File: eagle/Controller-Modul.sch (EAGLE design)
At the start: 53 parts, among them IC2 7805TV, Q6 BC550C, Q7 BC560, U1 ATTINY85-20S, X1 MKDSN1,5/2-5,08, X2 MKDSN1,5/2-5,08, X4 MKDSN1,5/2-5,08

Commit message: pcb design
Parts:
- removed C1, C5, C6: 100nF, rcl:C-EUC0805
- removed C2: 100µ, resistor:CPOL-EUE2.5-7
- removed C3: (no value), rcl:C-EUC0603K
- removed C4: 1000µ, rcl:CPOL-EUE3.5-8
- removed D1: 18V, diode:ZENER-DIODESOD80C
- removed D2: (no value), diode:ZENER-DIODESOT23
- removed D3: 1N4004, diode:1N4004
- removed IC1: (no value), v-reg:LM317TS
- removed IC2: 7805TV, linear:7805TV
- removed LED1: (no value), led:LED3MM
- removed Q2, Q3, Q4, Q5: (no value), transistor-power:PMOSFET_NTO220BV
- removed Q6: BC550C, transistor-npn:BC550C
- removed Q7: BC560, transistor-pnp:BC560
- removed R15: 1k, resistor:R-EU_R1206
- removed R16, R18, R19: 33k, resistor:R-EU_R1206
- removed R17: 10k, resistor:R-EU_R1206
- removed R20: 100k, rcl:R-EU_R1206
- removed R21: (no value), pot:TRIM_EU-PT10
- removed R5, R6, R7: (no value), resistor:R-EU_0207/10
- removed TR1, TR2: (no value), trafo:EI38-1
- removed U$1: GLEICHRICHTER, Gleichrichter:GLEICHRICHTER
- removed U1: ATTINY85-20S, _hhn_attiny25_45_85:ATTINY85-20S
- removed X1, X2, X4: MKDSN1,5/2-5,08, con-phoenix-508:MKDSN1,5/2-5,08
- added 1: SUMMER4, 0liver:SUMMER4
- added C10, C11: 22pF, resistor:C-EUC0603K
- added C12: 100 nF, resistor:C-EUC0603
- added C9: 1n, rcl:C-EUC0603K
- added D4, D5, D6: (no value), diode:ZENER-DIODESOT23
- added IC3: ATMEGA328P, avr-6:MEGA48/88/168-PU
- added JP10, JP4, JP6: (no value), pinhead:PINHD-1X2
- added JP5: (no value), pinhead:PINHD-1X4
- added JP7: (no value), pinhead:PINHD-1X16
- added JP8: (no value), pinhead:PINHD-2X3
- added JP9: (no value), pinhead:PINHD-1X3
- C7: value 100nF -> 1n; device rcl:C-EUC0805 -> rcl:C-EUC0603K
- C8: value 100µ -> 1n; device rcl:CPOL-EUE3.5-8 -> rcl:C-EUC0603K
- JP2: device pinhead:PINHD-2X3 -> pinhead:PINHD-1X2
- Q1: value (none) -> BC550C; device transistor-power:PMOSFET_NTO220BV -> transistor-npn:BC550C
- R10, R8: value (none) -> 300; device resistor:R-EU_0207/10 -> resistor:R-EU_R1206
- R11: value (none) -> 10k; device resistor:R-EU_0207/10 -> pot:TRIM_EU-PT10
- R12: value 100k -> 2k7; device rcl:R-EU_R1206 -> resistor:R-EU_R1206
- R13: value 10k -> 300
- R14: value 33k -> 2k7
- R2: value (none) -> 10k; device resistor:R-EU_0207/10 -> resistor:R-EU_R1206
- R3: value (none) -> 33k; device resistor:R-EU_0207/10 -> resistor:R-EU_R1206
- R4: value (none) -> 220; device resistor:R-EU_0207/10 -> resistor:R-EU_R1206
- R9: value (none) -> 2k7; device resistor:R-EU_0207/10 -> resistor:R-EU_R1206
- U$2: value GLEICHRICHTER -> ABRACON_ABM3_CRYSTALABM03_HC49; device Gleichrichter:GLEICHRICHTER -> Ava:ABRACON_ABM3_CRYSTALABM03_HC49
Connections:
- removed net +5V: C1.1, C6.1, IC2.VO, JP2.2, R12.2, U1.VCC
- removed net N$1: Q7.B, R13.2, R14.2
- removed net N$15: R15.1
- removed net N$16: Q1.D, Q2.D, Q3.D, Q4.D, Q5.D, R19.1
- removed net N$17: C4.+, C5.1, IC2.VI, U$1.+
- removed net N$19: TR1.P1, X4-1.KL
- removed net N$2: Q5.G, R11.1, R6.1
- removed net N$20: TR1.P2, X4-2.KL
- removed net N$21: TR1.S3, U$1.AC2
- removed net N$22: TR1.S4, U$1.AC1
- removed net N$23: R17.2, U1.PB3
- removed net N$25: U$2.AC2, X1-1.KL
- removed net N$29: JP1.2, R21.A
- removed net N$3: Q6.B, R16.2, R17.1
- removed net N$30: IC1.ADJ, JP1.1, R20.1
- removed net N$5: Q6.C, R13.1
- removed net N$7: Q3.G, R4.1, R9.1
- removed net N$8: C2.+, D1.C, Q7.E, R14.1, R15.2
- new net C1V: C7.2, D4.A, JP1.1, JP5.3, R8.1, R9.2
- new net C2V: C8.2, D5.A, JP5.1, R10.1, R12.2
- new net DATA0: IC3.PD2(INT0/PCINT18), JP7.11
- new net DATA1: IC3.PD3(INT1/OC2B/PCINT19), JP7.12
- new net DATA2: IC3.PD4(T0/XCK/PCINT20), JP7.13
- new net DATA3: IC3.PD5(T1/OC0B/PCINT21), JP7.14
- new net LED: IC3.PB0(ICP1/CLKO/PCINT0), R4.1
- new net N$26: IC3.PB1(OC1A/PCINT1), R1.2
- new net N$31: IC3.PD7(AIN1/PCINT23), JP9.2
- new net N$32: JP7.3, R11.S
- new net N$34: IC3.PD6(AIN0/OC0A/PCINT22), JP9.1
- new net N$47: JP7.15, R4.2
- new net RES: IC3.PC6(/RESET/PCINT14), JP8.5
- new net RS: IC3.PD0(RXD/PCINT16), JP7.4
- new net RW: IC3.PD1(TXD/PCINT17), JP7.6
- new net SENV: C9.2, D6.A, JP5.4, R13.1, R14.2
- new net VCC: C12.1, IC3.AREF, IC3.AVCC, IC3.VCC@1, JP10.2, JP7.2, JP8.2, Q1.C, R11.A
- net GND: now also 1.+, C10.2, C11.2, C12.2, IC3.AGND, IC3.GND@1, JP1.2, JP10.1, JP2.1, JP3.1, JP5.2, JP6.2, JP7.1, JP7.16, JP7.5, JP8.6, JP9.3, R11.E, R12.1, R14.1, R3.2, R9.1; no longer C1.2, C2.-, C3.2, C4.-, C5.2, C6.2, C7.2, C8.-, D1.A, D2.A, IC2.GND, JP2.6, JP3.2, LED1.C, Q6.E, R16.1, R18.1, R21.E, R21.S, U$1.-, U$2.-, U1.GND, X2-1.KL
- net MISO: now also IC3.PB4(MISO/PCINT4), JP8.1; no longer JP2.1, U1.PB1
- net MOSI: now also IC3.PB3(MOSI/OC2A/PCINT3), JP8.4; no longer JP2.4, U1.PB0
- net N$10: now also IC3.PC0(ADC0/PCINT8), JP2.2; no longer JP2.5, R12.1, U1.NRES/PB5
- net N$11: now also JP4.1, Q1.E; no longer Q1.S, Q2.S, Q3.S, Q4.S, Q5.S, R2.2, R3.2, R4.2, R5.2, R6.2
- net N$12: now also IC3.PC1(ADC1/PCINT9), JP3.2; no longer R1.2, U1.PB4
- net N$13: now also 1.-, JP4.2; no longer Q1.G, R2.1, R7.1
- net N$14: now also C7.1, D4.C, IC3.PC4(ADC4/SDA/PCINT12), R8.2; no longer C3.1, D2.C, R18.2, R19.2
- net N$18: now also C9.1, D6.C, IC3.PC2(ADC2/PCINT10), R13.2; no longer Q7.C, R10.2, R11.2, R7.2, R8.2, R9.2
- net N$24: now also C8.1, D5.C, IC3.PC3(ADC3/PCINT11), R10.2; no longer U$2.AC1, X1-2.KL
- net N$27: now also C11.1, IC3.PB7(XTAL2/TOSC2/PCINT7), U$2.2; no longer C7.1, C8.+, D3.C, IC1.IN, U$2.+
- net N$28: now also C10.1, IC3.PB6(XTAL1/TOSC1/PCINT6), U$2.1; no longer D3.A, IC1.OUT, JP3.1, R20.2, X2-2.KL
- net N$4: now also Q1.B, R2.2; no longer Q4.G, R10.1, R5.1
- net N$6: now also JP6.1; no longer LED1.A
- net N$9: now also IC3.PB2(SS/OC1B/PCINT2), R2.1; no longer Q2.G, R8.1
- net SCK: now also IC3.PB5(SCK/PCINT5), JP8.3; no longer JP2.3, U1.PB2
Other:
- note added: "5V Vcc"
- note added: "AutoSchalter"
- note added: "Con: Kondensator Supply"
- note added: "FET Treiber"
- note added: "Fußtaster"
- note added: "LED"
- note added: "SDA"
- note added: "Voltmeter"
- note added: "Volume"
- note removed: "ISP"
- moved on the sheet: C7, JP1, JP3, R1, R10, R12, R13, R14, R2, R3, R4, R8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

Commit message: Lots of schema and board changes
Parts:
- added JP11: (no value), pinhead:PINHD-1X2
- added R5: 150, rcl:R-EU_R1206
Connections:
- new net N$1: JP11.1, R5.1
- new net N$2: IC3.PC5(ADC5/SCLPCINT13), R5.2
- net GND: now also JP11.2
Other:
- note added: "LED2"
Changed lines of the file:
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@@
 <part name="JP9" library="pinhead" deviceset="PINHD-1X3" device=""/>
 <part name="GND2" library="supply1" deviceset="GND" device=""/>
+<part name="R5" library="rcl" deviceset="R-EU_" device="R1206" value="150"/>
+<part name="GND1" library="supply1" deviceset="GND" device=""/>
+<part name="JP11" library="pinhead" deviceset="PINHD-1X2" device=""/>
 </parts>
 <sheets>
@@
 <text x="144.78" y="53.34" size="1.778" layer="97">AutoSchalter</text>
 <text x="248.92" y="2.54" size="1.778" layer="97">FET Treiber</text>
+<text x="172.72" y="20.32" size="1.778" layer="97">LED2</text>
 </plain>
 <instances>
@@
 <instance part="JP9" gate="A" x="251.46" y="10.16"/>
 <instance part="GND2" gate="1" x="238.76" y="-2.54"/>
+<instance part="R5" gate="G$1" x="160.02" y="38.1" rot="R180"/>
+<instance part="GND1" gate="1" x="165.1" y="17.78"/>
+<instance part="JP11" gate="G$1" x="177.8" y="25.4"/>
 </instances>
 <busses>
@@
 <wire x1="238.76" y1="5.08" x2="238.76" y2="0" width="0.1524" layer="91"/>
 <pinref part="GND2" gate="1" pin="GND"/>
+</segment>
+<segment>
+<pinref part="GND1" gate="1" pin="GND"/>
+<wire x1="165.1" y1="22.86" x2="165.1" y2="20.32" width="0.1524" layer="91"/>
+<wire x1="165.1" y1="22.86" x2="165.1" y2="25.4" width="0.1524" layer="91"/>
+<pinref part="JP11" gate="G$1" pin="2"/>
+<wire x1="165.1" y1="25.4" x2="175.26" y2="25.4" width="0.1524" layer="91"/>
 </segment>
 </net>
@@
 </segment>
 </net>
+<net name="N$1" class="0">
+<segment>
+<pinref part="R5" gate="G$1" pin="1"/>
+<wire x1="165.1" y1="38.1" x2="165.1" y2="30.48" width="0.1524" layer="91"/>
+<pinref part="JP11" gate="G$1" pin="1"/>
+<wire x1="175.26" y1="27.94" x2="165.1" y2="27.94" width="0.1524" layer="91"/>
+<wire x1="165.1" y1="27.94" x2="165.1" y2="30.48" width="0.1524" layer="91"/>
+</segment>
+</net>
+<net name="N$2" class="0">
+<segment>
+<pinref part="R5" gate="G$1" pin="2"/>
+<pinref part="IC3" gate="1" pin="PC5(ADC5/SCLPCINT13)"/>
+<wire x1="154.94" y1="38.1" x2="124.46" y2="38.1" width="0.1524" layer="91"/>
+</segment>
+</net>

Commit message: Var. Changes. Layout and new diode for 7818
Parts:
- removed C8, C9: 1n, rcl:C-EUC0603K
- removed D5, D6: (no value), diode:ZENER-DIODESOT23
- removed R10, R13: 300, resistor:R-EU_R1206
- removed R12, R14: 2k7, resistor:R-EU_R1206
- added C1, C2: 1n, rcl:C-EUC0603K
- added D1, D2: (no value), diode:ZENER-DIODESOT23
- added R15, R6: 560, resistor:R-EU_R1206
- added R16, R7: 3k9, resistor:R-EU_R1206
- JP9: device pinhead:PINHD-1X3 -> pinhead:PINHD-1X4
- R2: value 10k -> 1k
- R8: value 300 -> 560
- R9: value 2k7 -> 3k9
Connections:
- removed net N$14: C7.1, D4.C, IC3.PC4(ADC4/SDA/PCINT12), R8.2
- removed net N$24: C8.1, D5.C, IC3.PC3(ADC3/PCINT11), R10.2
- new net N$5: C7.2, D4.A, IC3.PC4(ADC4/SDA/PCINT12), R8.1, R9.2
- new net N$7: C1.2, D1.A, IC3.PC3(ADC3/PCINT11), R6.1, R7.2
- net C1V: now also R9.1; no longer C7.2, D4.A, R8.1, R9.2
- net C2V: now also R7.1; no longer C8.2, D5.A, R10.1, R12.2
- net GND: now also C1.1, C2.1, C7.1, D1.C, D2.C, D4.C, JP9.4, R15.2, R6.2, R8.2; no longer JP9.3, R12.1, R14.1, R9.1
- net MISO: now also JP9.1
- net N$18: now also C2.2, D2.A, R15.1, R16.2; no longer C9.1, D6.C, R13.2
- net N$31: now also JP9.3; no longer JP9.2
- net N$34: now also JP9.2; no longer JP9.1
- net SENV: now also R16.1; no longer C9.2, D6.A, R13.1, R14.2
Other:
- moved on the sheet: C7, D4, JP1, R8, R9

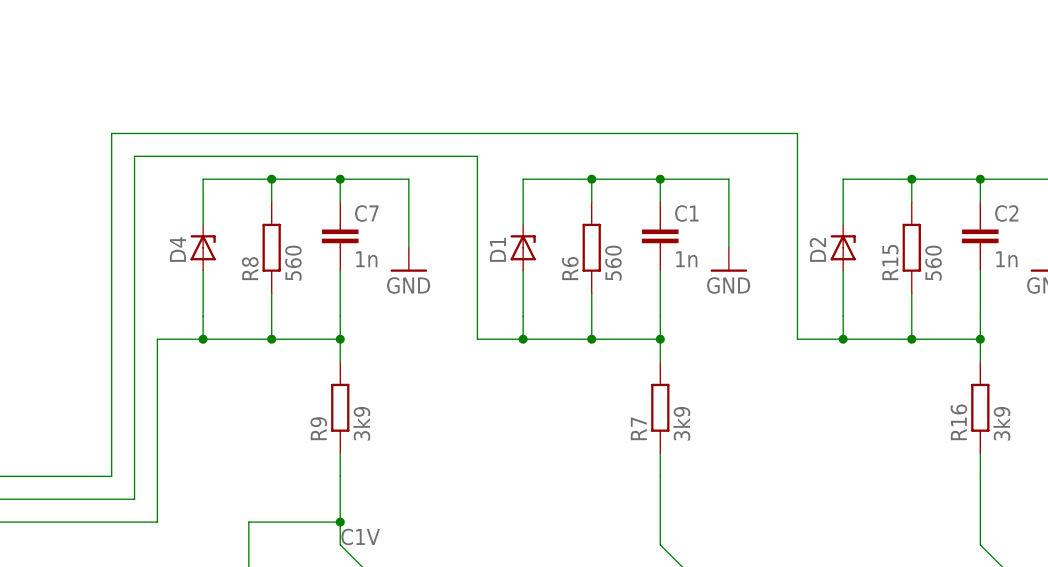
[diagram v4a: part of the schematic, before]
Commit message: Corrected wrong direction of zener diodes
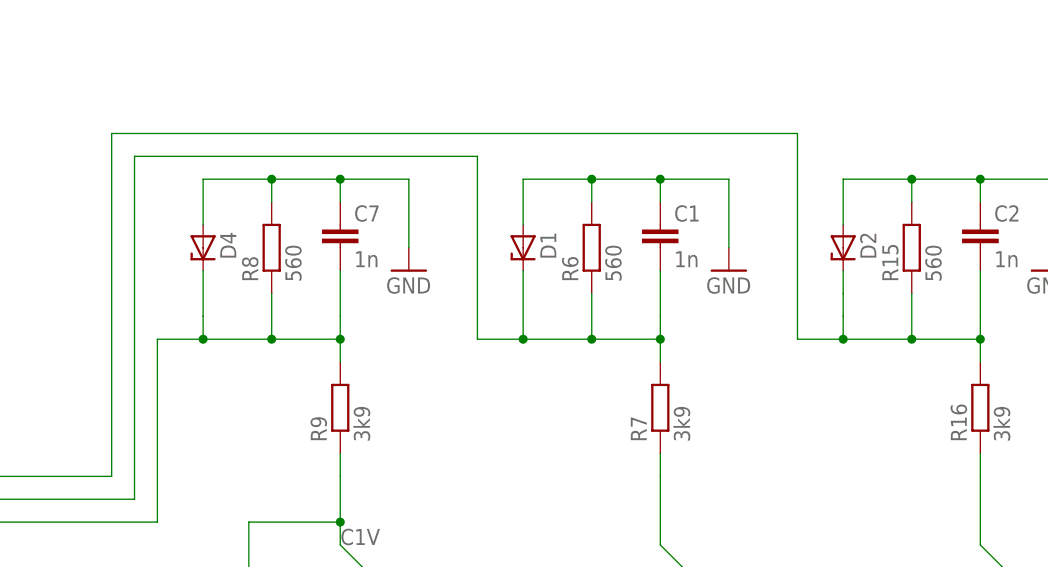
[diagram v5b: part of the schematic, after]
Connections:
- net GND: now also D1.A, D2.A, D4.A; no longer D1.C, D2.C, D4.C
- net N$18: now also D2.C; no longer D2.A
- net N$5: now also D4.C; no longer D4.A
- net N$7: now also D1.C; no longer D1.A
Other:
- moved on the sheet: D1, D2, D4
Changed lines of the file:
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@@
 <instance part="JP3" gate="G$1" x="170.18" y="60.96"/>
 <instance part="GND8" gate="1" x="157.48" y="58.42"/>
-<instance part="D4" gate="G$1" x="203.2" y="71.12" rot="R90"/>
+<instance part="D4" gate="G$1" x="203.2" y="71.12" rot="R270"/>
 <instance part="R8" gate="G$1" x="210.82" y="71.12" rot="R90"/>
 <instance part="C7" gate="G$1" x="218.44" y="73.66"/>
@@
 <instance part="GND1" gate="1" x="165.1" y="17.78"/>
 <instance part="JP11" gate="G$1" x="177.8" y="25.4"/>
-<instance part="D1" gate="G$1" x="238.76" y="71.12" rot="R90"/>
+<instance part="D1" gate="G$1" x="238.76" y="71.12" rot="R270"/>
 <instance part="R6" gate="G$1" x="246.38" y="71.12" rot="R90"/>
 <instance part="C1" gate="G$1" x="254" y="73.66"/>
 <instance part="R7" gate="G$1" x="254" y="53.34" rot="R90"/>
 <instance part="GND4" gate="1" x="261.62" y="68.58"/>
-<instance part="D2" gate="G$1" x="274.32" y="71.12" rot="R90"/>
+<instance part="D2" gate="G$1" x="274.32" y="71.12" rot="R270"/>
 <instance part="R15" gate="G$1" x="281.94" y="71.12" rot="R90"/>
 <instance part="C2" gate="G$1" x="289.56" y="73.66"/>
@@
 </segment>
 <segment>
-<pinref part="D4" gate="G$1" pin="C"/>
 <pinref part="R8" gate="G$1" pin="2"/>
 <pinref part="C7" gate="G$1" pin="1"/>
@@
 <junction x="210.82" y="78.74"/>
 <wire x1="210.82" y1="78.74" x2="203.2" y2="78.74" width="0.1524" layer="91"/>
-<wire x1="203.2" y1="78.74" x2="203.2" y2="73.66" width="0.1524" layer="91"/>
 <pinref part="GND9" gate="1" pin="GND"/>
 <wire x1="218.44" y1="78.74" x2="226.06" y2="78.74" width="0.1524" layer="91"/>
 <wire x1="226.06" y1="78.74" x2="226.06" y2="71.12" width="0.1524" layer="91"/>
 <junction x="218.44" y="78.74"/>
-</segment>
-<segment>
-<pinref part="D1" gate="G$1" pin="C"/>
+<pinref part="D4" gate="G$1" pin="A"/>
+<wire x1="203.2" y1="78.74" x2="203.2" y2="73.66" width="0.1524" layer="91"/>
+</segment>
+<segment>
 <pinref part="R6" gate="G$1" pin="2"/>
 <pinref part="C1" gate="G$1" pin="1"/>
@@
 <junction x="246.38" y="78.74"/>
 <wire x1="246.38" y1="78.74" x2="238.76" y2="78.74" width="0.1524" layer="91"/>
-<wire x1="238.76" y1="78.74" x2="238.76" y2="73.66" width="0.1524" layer="91"/>
 <pinref part="GND4" gate="1" pin="GND"/>
 <wire x1="254" y1="78.74" x2="261.62" y2="78.74" width="0.1524" layer="91"/>
 <wire x1="261.62" y1="78.74" x2="261.62" y2="71.12" width="0.1524" layer="91"/>
 <junction x="254" y="78.74"/>
-</segment>
-<segment>
-<pinref part="D2" gate="G$1" pin="C"/>
+<pinref part="D1" gate="G$1" pin="A"/>
+<wire x1="238.76" y1="78.74" x2="238.76" y2="73.66" width="0.1524" layer="91"/>
+</segment>
+<segment>
 <pinref part="R15" gate="G$1" pin="2"/>
 <pinref part="C2" gate="G$1" pin="1"/>
@@
 <junction x="281.94" y="78.74"/>
 <wire x1="281.94" y1="78.74" x2="274.32" y2="78.74" width="0.1524" layer="91"/>
-<wire x1="274.32" y1="78.74" x2="274.32" y2="73.66" width="0.1524" layer="91"/>
 <pinref part="GND5" gate="1" pin="GND"/>
 <wire x1="289.56" y1="78.74" x2="297.18" y2="78.74" width="0.1524" layer="91"/>
 <wire x1="297.18" y1="78.74" x2="297.18" y2="71.12" width="0.1524" layer="91"/>
 <junction x="289.56" y="78.74"/>
+<pinref part="D2" gate="G$1" pin="A"/>
+<wire x1="274.32" y1="78.74" x2="274.32" y2="73.66" width="0.1524" layer="91"/>
 </segment>
 </net>
@@
 <wire x1="193.04" y1="45.72" x2="193.04" y2="83.82" width="0.1524" layer="91"/>
 <wire x1="193.04" y1="83.82" x2="269.24" y2="83.82" width="0.1524" layer="91"/>
-<pinref part="D2" gate="G$1" pin="A"/>
-<wire x1="274.32" y1="63.5" x2="274.32" y2="68.58" width="0.1524" layer="91"/>
 <wire x1="289.56" y1="60.96" x2="281.94" y2="60.96" width="0.1524" layer="91"/>
 <wire x1="281.94" y1="60.96" x2="274.32" y2="60.96" width="0.1524" layer="91"/>
@@
 <junction x="289.56" y="60.96"/>
 <wire x1="269.24" y1="83.82" x2="269.24" y2="60.96" width="0.1524" layer="91"/>
+<wire x1="274.32" y1="66.04" x2="274.32" y2="63.5" width="0.1524" layer="91"/>
+<pinref part="D2" gate="G$1" pin="C"/>
+<wire x1="274.32" y1="66.04" x2="274.32" y2="68.58" width="0.1524" layer="91"/>
 </segment>
 </net>
@@
 <net name="N$5" class="0">
 <segment>
-<pinref part="D4" gate="G$1" pin="A"/>
-<wire x1="203.2" y1="63.5" x2="203.2" y2="68.58" width="0.1524" layer="91"/>
 <wire x1="218.44" y1="60.96" x2="210.82" y2="60.96" width="0.1524" layer="91"/>
 <wire x1="210.82" y1="60.96" x2="203.2" y2="60.96" width="0.1524" layer="91"/>
@@
 <wire x1="218.44" y1="58.42" x2="218.44" y2="60.96" width="0.1524" layer="91"/>
 <junction x="218.44" y="60.96"/>
+<pinref part="D4" gate="G$1" pin="C"/>
+<wire x1="203.2" y1="68.58" x2="203.2" y2="63.5" width="0.1524" layer="91"/>
 </segment>
 </net>
 <net name="N$7" class="0">
 <segment>
-<pinref part="D1" gate="G$1" pin="A"/>
-<wire x1="238.76" y1="63.5" x2="238.76" y2="68.58" width="0.1524" layer="91"/>
 <wire x1="254" y1="60.96" x2="246.38" y2="60.96" width="0.1524" layer="91"/>
 <wire x1="246.38" y1="60.96" x2="238.76" y2="60.96" width="0.1524" layer="91"/>
-<wire x1="238.76" y1="63.5" x2="238.76" y2="60.96" width="0.1524" layer="91"/>
 <pinref part="R6" gate="G$1" pin="1"/>
 <wire x1="246.38" y1="66.04" x2="246.38" y2="60.96" width="0.1524" layer="91"/>
@@
 <wire x1="254" y1="60.96" x2="254" y2="63.5" width="0.1524" layer="91"/>
 <wire x1="238.76" y1="60.96" x2="233.68" y2="60.96" width="0.1524" layer="91"/>
-<junction x="238.76" y="60.96"/>
 <wire x1="254" y1="58.42" x2="254" y2="60.96" width="0.1524" layer="91"/>
 <junction x="254" y="60.96"/>
@@
 <wire x1="195.58" y1="43.18" x2="195.58" y2="81.28" width="0.1524" layer="91"/>
 <wire x1="233.68" y1="81.28" x2="195.58" y2="81.28" width="0.1524" layer="91"/>
-</segment>
-</net>
+<pinref part="D1" gate="G$1" pin="C"/>
+<wire x1="238.76" y1="68.58" x2="238.76" y2="60.96" width="0.1524" layer="91"/>
+<junction x="238.76" y="60.96"/>
+</segment>
+</net>
